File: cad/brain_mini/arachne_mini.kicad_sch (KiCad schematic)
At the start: 86 parts, among them J1 12V IN, J13 5V PI, J2 L1 servo, J3 L2 servo, J4 L3 servo, J5 L4 servo, J6 L5 servo, J7 L6 servo, J8 USB-C PI, Q1 AOD4185, SW1 RESET, SW2 BOOT, U1 TPS54560B, U10 USBLC6-2SC6, U2 AMS1117-3.3, U3 ESP32-S3-WROOM-1-N16R8, U4 74AHCT1G126, U5 74LVC1G34, U6 74AHCT1G126, U7 74LVC1G34, U8 MPU-6050

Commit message: Mini board: 2x13 GPIO header with all 19 free ESP32-S3 GPIOs + I2C + power, IMU moved
Co-Authored-By: Claude Opus 5.5 <noreply@anthropic.com>
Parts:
- added J14: GPIO, arachne:PinHeader_2x13_P2.54mm_Vertical, symbol arachne:Conn_02x13_Odd_Even
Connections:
- net 3V3: now also J14.1 (Pin_1)
- net GND: now also J14.26 (Pin_26), J14.3 (Pin_3), J14.4 (Pin_4)
- net IMU_SCL: now also J14.6 (Pin_6)
- net IMU_SDA: now also J14.5 (Pin_5)
- net V5: now also J14.2 (Pin_2)
- net IO8: now reaches U3.12 (IO8)
- net IO8: now also J14.9 (Pin_9)
- net IO3: now reaches U3.15 (IO3)
- net IO3: now also J14.10 (Pin_10)
- net IO46: now reaches U3.16 (IO46)
- net IO46: now also J14.11 (Pin_11)
- net IO12: now reaches U3.20 (IO12)
- net IO12: now also J14.12 (Pin_12)
- net IO13: now reaches U3.21 (IO13)
- net IO13: now also J14.13 (Pin_13)
- net IO14: now reaches U3.22 (IO14)
- net IO14: now also J14.14 (Pin_14)
- net IO21: now reaches U3.23 (IO21)
- net IO21: now also J14.15 (Pin_15)
- net IO47: now reaches U3.24 (IO47)
- net IO47: now also J14.16 (Pin_16)
- net IO48: now reaches U3.25 (IO48)
- net IO48: now also J14.17 (Pin_17)
- net IO45: now reaches U3.26 (IO45)
- net IO45: now also J14.18 (Pin_18)
- net IO38: now reaches U3.31 (IO38)
- net IO38: now also J14.19 (Pin_19)
- net IO39: now reaches U3.32 (IO39)
- net IO39: now also J14.20 (Pin_20)
- net IO40: now reaches U3.33 (IO40)
- net IO40: now also J14.21 (Pin_21)
- net IO41: now reaches U3.34 (IO41)
- net IO41: now also J14.22 (Pin_22)
- net IO42: now reaches U3.35 (IO42)
- net IO42: now also J14.23 (Pin_23)
- net IO44: now reaches U3.36 (RXD0)
- net IO44: now also J14.25 (Pin_25)
- net IO43: now reaches U3.37 (TXD0)
- net IO43: now also J14.24 (Pin_24)
- net IO7: now reaches U3.7 (IO7)
- net IO7: now also J14.7 (Pin_7)
- net IO15: now reaches U3.8 (IO15)
- net IO15: now also J14.8 (Pin_8)
- no-connect marks 39 -> 20
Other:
- note added: "GPIO HEADER"
- moved on the sheet: H1, H2, H3, H4

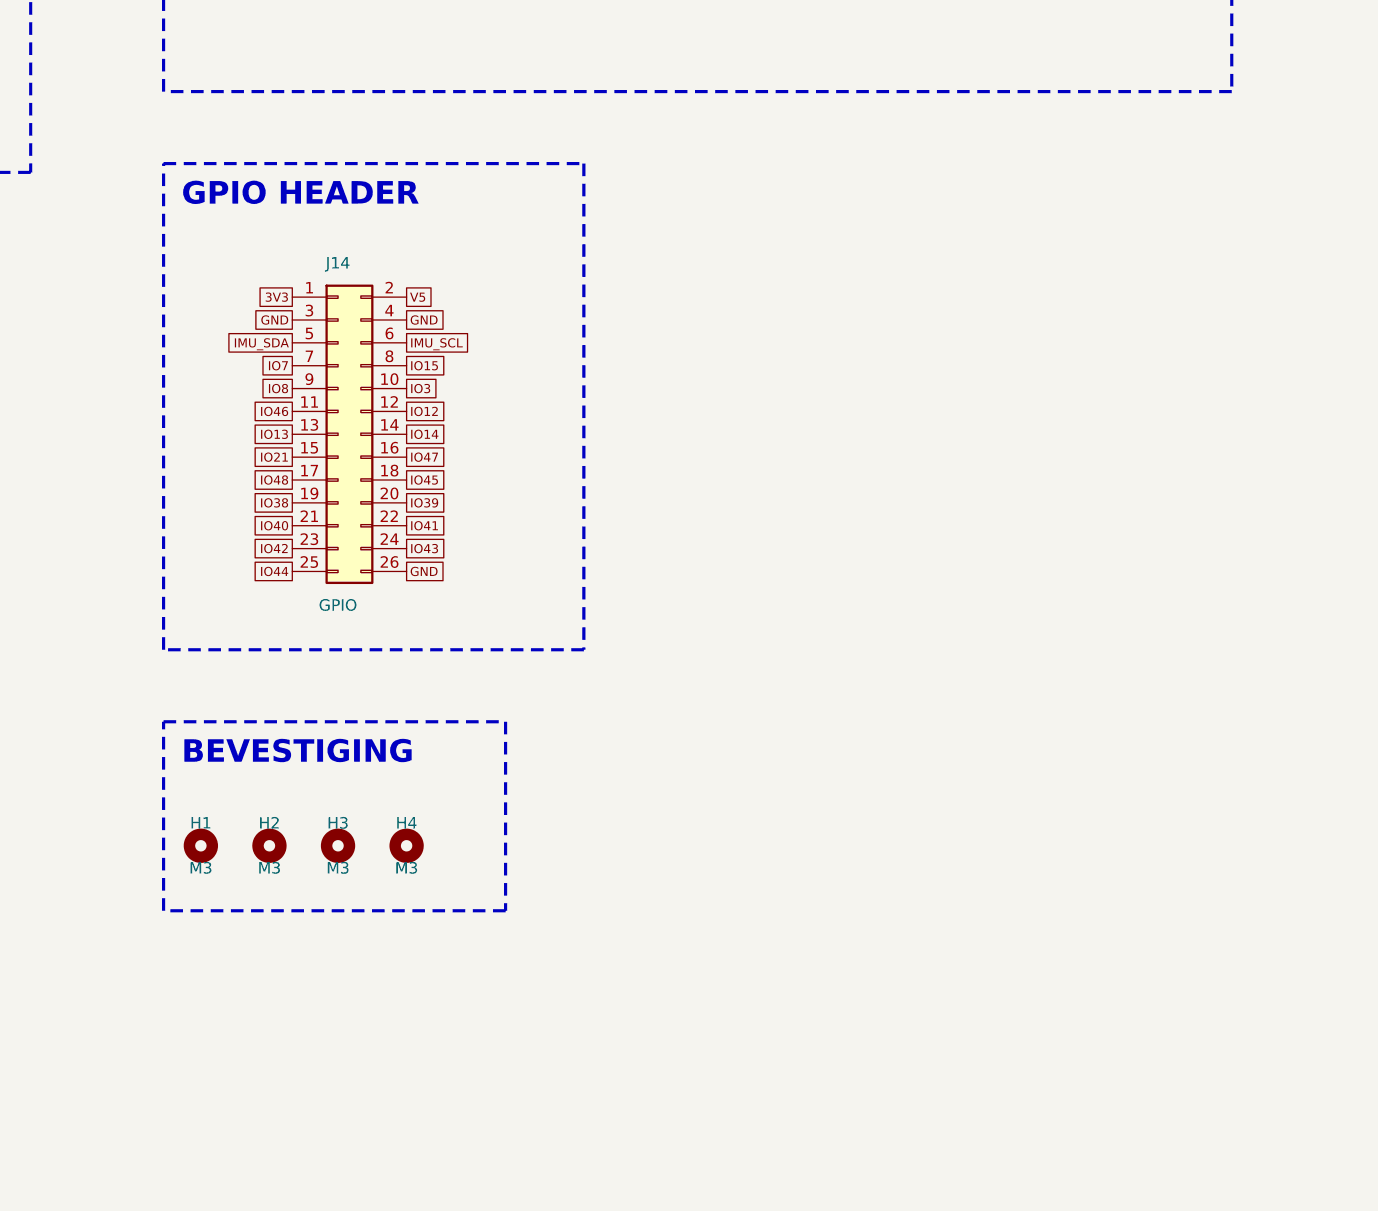
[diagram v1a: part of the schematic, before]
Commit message: Mini board: sensor strip (G-V-S per GPIO) on a 10 mm longer bottom edge, 2x Qwiic, USB-C moved to the new edge
Co-Authored-By: Claude Opus 5.5 <noreply@anthropic.com>
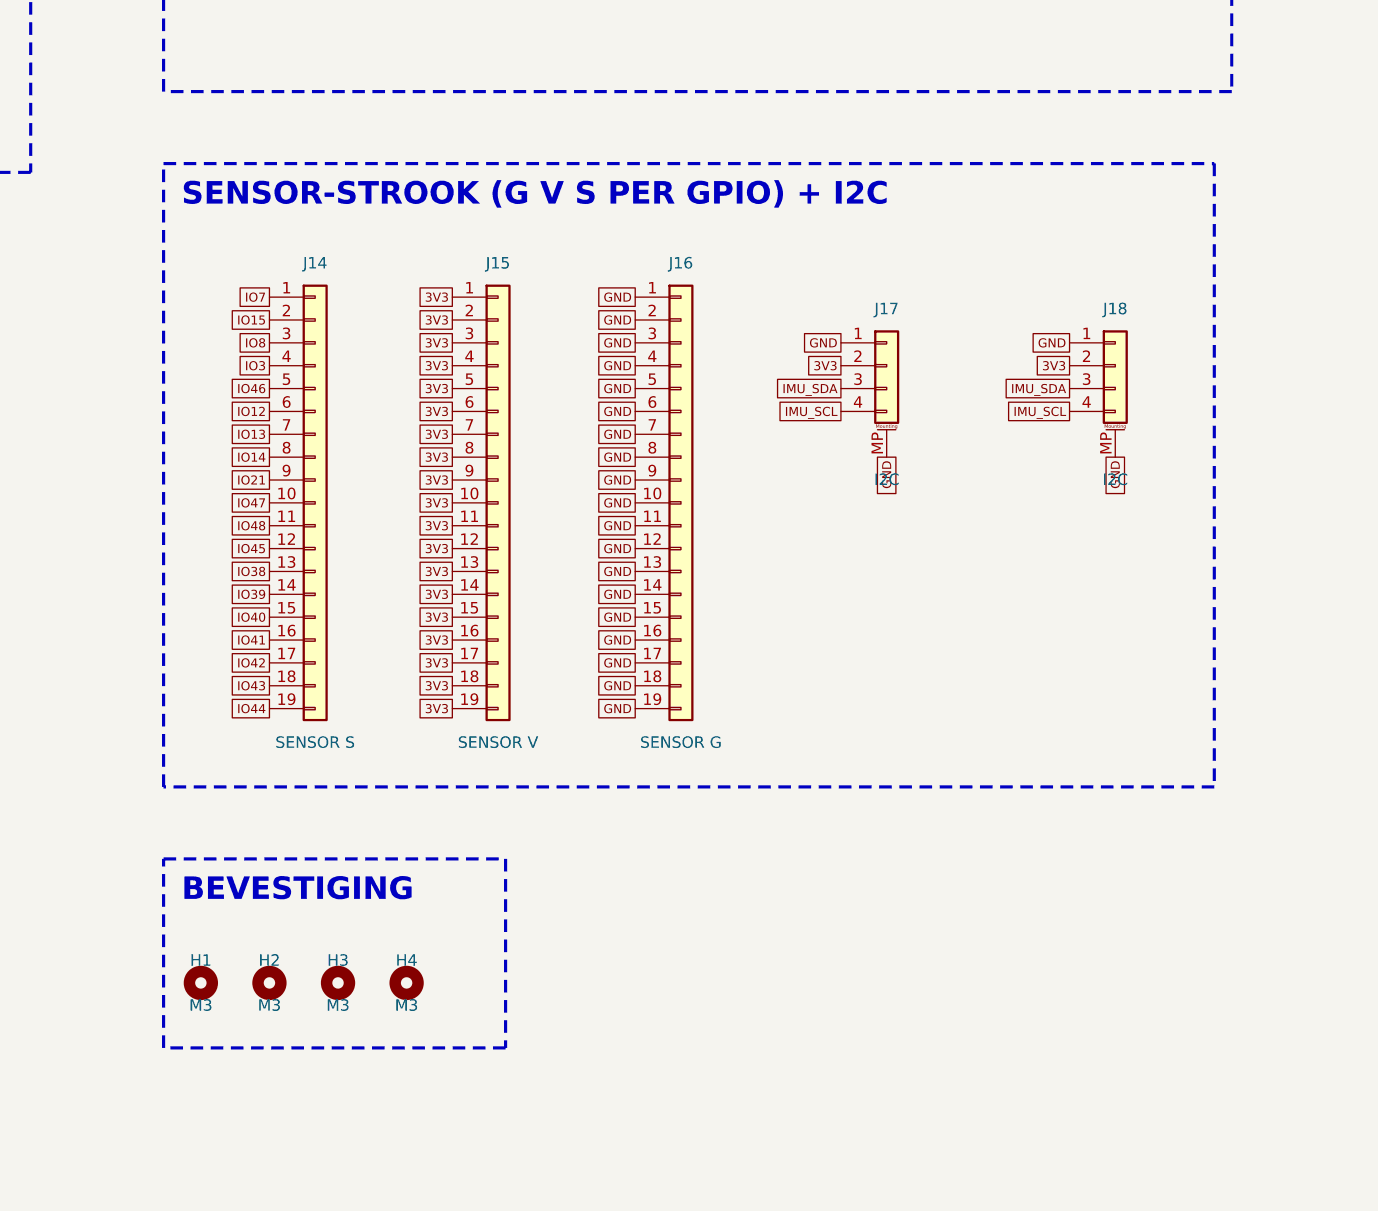
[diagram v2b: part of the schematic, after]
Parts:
- added J15: SENSOR V, arachne:PinHeader_1x19_P2.54mm_Vertical, symbol arachne:Conn_01x19
- added J16: SENSOR G, arachne:PinHeader_1x19_P2.54mm_Vertical, symbol arachne:Conn_01x19
- added J17, J18: I2C, arachne:JST_SH_SM04B-SRSS-TB_1x04-1MP_P1.00mm_Horizontal, symbol arachne:Conn_01x04_MountingPin
- J14: value GPIO -> SENSOR S; footprint arachne:PinHeader_2x13_P2.54mm_Vertical -> arachne:PinHeader_1x19_P2.54mm_Vertical; symbol arachne:Conn_02x13_Odd_Even -> arachne:Conn_01x19; MPN 2x13 pin header 2.54 mm: 19 free ESP32-S3 GPIOs + I2C + 3V3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 -> 1x19 pin header 2.54 mm (row S of the sensor strip)
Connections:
- net 3V3: now also J15.1 (Pin_1), J15.10 (Pin_10), J15.11 (Pin_11), J15.12 (Pin_12), J15.13 (Pin_13), J15.14 (Pin_14), J15.15 (Pin_15), J15.16 (Pin_16), J15.17 (Pin_17), J15.18 (Pin_18), J15.19 (Pin_19), J15.2 (Pin_2), J15.3 (Pin_3), J15.4 (Pin_4), J15.5 (Pin_5), J15.6 (Pin_6), J15.7 (Pin_7), J15.8 (Pin_8), J15.9 (Pin_9), J17.2 (Pin_2), J18.2 (Pin_2); no longer J14.1 (Pin_1)
- net GND: now also J16.1 (Pin_1), J16.10 (Pin_10), J16.11 (Pin_11), J16.12 (Pin_12), J16.13 (Pin_13), J16.14 (Pin_14), J16.15 (Pin_15), J16.16 (Pin_16), J16.17 (Pin_17), J16.18 (Pin_18), J16.19 (Pin_19), J16.2 (Pin_2), J16.3 (Pin_3), J16.4 (Pin_4), J16.5 (Pin_5), J16.6 (Pin_6), J16.7 (Pin_7), J16.8 (Pin_8), J16.9 (Pin_9), J17.1 (Pin_1), J17.MP (MountPin), J18.1 (Pin_1), J18.MP (MountPin); no longer J14.26 (Pin_26), J14.3 (Pin_3), J14.4 (Pin_4)
- net IMU_SCL: now also J17.4 (Pin_4), J18.4 (Pin_4); no longer J14.6 (Pin_6)
- net IMU_SDA: now also J17.3 (Pin_3), J18.3 (Pin_3); no longer J14.5 (Pin_5)
- net IO12: now also J14.6 (Pin_6); no longer J14.12 (Pin_12)
- net IO13: now also J14.7 (Pin_7); no longer J14.13 (Pin_13)
- net IO14: now also J14.8 (Pin_8); no longer J14.14 (Pin_14)
- net IO15: now also J14.2 (Pin_2); no longer J14.8 (Pin_8)
- net IO21: now also J14.9 (Pin_9); no longer J14.15 (Pin_15)
- net IO3: now also J14.4 (Pin_4); no longer J14.10 (Pin_10)
- net IO38: now also J14.13 (Pin_13); no longer J14.19 (Pin_19)
- net IO39: now also J14.14 (Pin_14); no longer J14.20 (Pin_20)
- net IO40: now also J14.15 (Pin_15); no longer J14.21 (Pin_21)
- net IO41: now also J14.16 (Pin_16); no longer J14.22 (Pin_22)
- net IO42: now also J14.17 (Pin_17); no longer J14.23 (Pin_23)
- net IO43: now also J14.18 (Pin_18); no longer J14.24 (Pin_24)
- net IO44: now also J14.19 (Pin_19); no longer J14.25 (Pin_25)
- net IO45: now also J14.12 (Pin_12); no longer J14.18 (Pin_18)
- net IO46: now also J14.5 (Pin_5); no longer J14.11 (Pin_11)
- net IO47: now also J14.10 (Pin_10); no longer J14.16 (Pin_16)
- net IO48: now also J14.11 (Pin_11); no longer J14.17 (Pin_17)
- net IO7: now also J14.1 (Pin_1); no longer J14.7 (Pin_7)
- net IO8: now also J14.3 (Pin_3); no longer J14.9 (Pin_9)
- net V5: no longer J14.2 (Pin_2)
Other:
- note added: "SENSOR-STROOK (G V S PER GPIO) + I2C"
- note removed: "GPIO HEADER"
- moved on the sheet: H1, H2, H3, H4

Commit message: Mini board: servo headers are now Molex Mini-SPOX 5267-03A (chamfered, mates with the 5264 plug), real Molex in the BOM
Co-Authored-By: Claude Opus 5.5 <noreply@anthropic.com>
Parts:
- J2, J3, J4, J5, J6, J7: footprint arachne:Molex_5268-03A_1x03_P2.50mm_Vertical -> arachne:Molex_5267-03A_1x03_P2.50mm_Vertical; MPN Molex 5268-03A (5264 mating, Feetech bus) -> Molex 22-03-5035 / 5267-03A Mini-SPOX (mates with the 5264 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
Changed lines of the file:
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@@
 			)
 		)
-		(property "Footprint" "arachne:Molex_5268-03A_1x03_P2.50mm_Vertical"
+		(property "Footprint" "arachne:Molex_5267-03A_1x03_P2.50mm_Vertical"
 			(at 33.02 403.86 0)
 			(effects
@@
 			)
 		)
-		(property "MPN" "Molex 5268-03A (5264 mating, Feetech bus)"
+		(property "MPN" "Molex 22-03-5035 / 5267-03A Mini-SPOX (mates with the 5264 plug on Feetech cables)"
 			(at 33.02 403.86 0)
 			(effects
@@
 			)
 		)
-		(property "Footprint" "arachne:Molex_5268-03A_1x03_P2.50mm_Vertical"
+		(property "Footprint" "arachne:Molex_5267-03A_1x03_P2.50mm_Vertical"
 			(at 53.34 403.86 0)
 			(effects
@@
 			)
 		)
-		(property "MPN" "Molex 5268-03A (5264 mating, Feetech bus)"
+		(property "MPN" "Molex 22-03-5035 / 5267-03A Mini-SPOX (mates with the 5264 plug on Feetech cables)"
 			(at 53.34 403.86 0)
 			(effects
@@
 			)
 		)
-		(property "Footprint" "arachne:Molex_5268-03A_1x03_P2.50mm_Vertical"
+		(property "Footprint" "arachne:Molex_5267-03A_1x03_P2.50mm_Vertical"
 			(at 76.2 403.86 0)
 			(effects
@@
 			)
 		)
-		(property "MPN" "Molex 5268-03A (5264 mating, Feetech bus)"
+		(property "MPN" "Molex 22-03-5035 / 5267-03A Mini-SPOX (mates with the 5264 plug on Feetech cables)"
 			(at 76.2 403.86 0)
 			(effects
@@
 			)
 		)
-		(property "Footprint" "arachne:Molex_5268-03A_1x03_P2.50mm_Vertical"
+		(property "Footprint" "arachne:Molex_5267-03A_1x03_P2.50mm_Vertical"
 			(at 33.02 482.6 0)
 			(effects
@@
 			)
 		)
-		(property "MPN" "Molex 5268-03A (5264 mating, Feetech bus)"
+		(property "MPN" "Molex 22-03-5035 / 5267-03A Mini-SPOX (mates with the 5264 plug on Feetech cables)"
 			(at 33.02 482.6 0)
 			(effects
@@
 			)
 		)
-		(property "Footprint" "arachne:Molex_5268-03A_1x03_P2.50mm_Vertical"
+		(property "Footprint" "arachne:Molex_5267-03A_1x03_P2.50mm_Vertical"
 			(at 53.34 482.6 0)
 			(effects
@@
 			)
 		)
-		(property "MPN" "Molex 5268-03A (5264 mating, Feetech bus)"
+		(property "MPN" "Molex 22-03-5035 / 5267-03A Mini-SPOX (mates with the 5264 plug on Feetech cables)"
 			(at 53.34 482.6 0)
 			(effects
@@
 			)
 		)
-		(property "Footprint" "arachne:Molex_5268-03A_1x03_P2.50mm_Vertical"
+		(property "Footprint" "arachne:Molex_5267-03A_1x03_P2.50mm_Vertical"
 			(at 76.2 482.6 0)
 			(effects
@@
 			)
 		)
-		(property "MPN" "Molex 5268-03A (5264 mating, Feetech bus)"
+		(property "MPN" "Molex 22-03-5035 / 5267-03A Mini-SPOX (mates with the 5264 plug on Feetech cables)"
 			(at 76.2 482.6 0)
 			(effects

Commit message: Name Kobe Vanrobaeys on silkscreen/schematic, fresh JLC fab files for brain_mini
Co-Authored-By: Claude Opus 5.5 <noreply@anthropic.com>
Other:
- company: Kobe Van Robaeys - maakleerplek -> Kobe Vanrobaeys - maakleerplek
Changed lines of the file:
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@@
 		(date "2026-10-18")
 		(rev "1.0")
-		(company "Kobe Van Robaeys - maakleerplek")
+		(company "Kobe Vanrobaeys - maakleerplek")
 		(comment 1 "ESP32-S3 + MPU-6050, 6 servo-bus legs, USB to Pi 4")
 	)

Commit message: brain_mini v4 price pass: JLC basic parts (buck network, caps, SS54, LEDs), LSM6DS3TR-C IMU, hand-solder parts DNP, JLC rotation corrections in the CPL
Co-Authored-By: Claude Opus 5.5 <noreply@anthropic.com>
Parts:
- removed C25: 2n2, arachne:C_0603_1608Metric, symbol arachne:C
- removed C27: 10n, arachne:C_0603_1608Metric, symbol arachne:C
- C1, C2: MPN 330uF 25V 8x10.5 alu -> hand-solder (not placed by JLC): 330uF 25V 8x10.5 alu, STRO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; now not fitted
- C10, C11, C9: footprint arachne:C_1210_3225Metric -> arachne:C_1206_3216Metric; MPN 1210 47u 10V X5R ceramic -> 1206 47u 10V X5R ceramic
- C3, C5, C6: footprint arachne:C_1206_3216Metric -> arachne:C_0805_2012Metric; MPN 1206 10u 25V X5R ceramic -> 0805 10u 25V X5R ceramic
- D1: MPN SMBJ15CA -> hand-solder (not placed by JLC): SMBJ15CA TVS (optional); now not fitted
- D2: MPN BZT52C15 (gate clamp) -> hand-solder (not placed by JLC): BZT52C15 gate clamp (optio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; now not fitted
- D4: value B560C -> SS54; footprint arachne:D_SMC -> arachne:D_SMA; MPN B560C (5 A 60 V Schottky) -> SS54 (5 A 40 V Schottky, JLC basic)
- D5: value groen 5V -> LED 5V; MPN LED 0603 green -> LED 0603 red (JLC basic)
- D8: value blauw ESP -> LED ESP; MPN LED 0603 blue -> LED 0603 red (JLC basic)
- J14: MPN 1x19 pin header 2.54 mm (row S of the sensor strip) -> hand-solder (not placed by JLC): 1x19 pin header 2.54 mm (r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; now not fitted
- J15: MPN 1x19 pin header 2.54 mm (row V of the sensor strip) -> hand-solder (not placed by JLC): 1x19 pin header 2.54 mm (r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; now not fitted
- J16: MPN 1x19 pin header 2.54 mm (row G of the sensor strip) -> hand-solder (not placed by JLC): 1x19 pin header 2.54 mm (r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; now not fitted
- J17, J18: MPN JST SM04B-SRSS-TB (Qwiic / STEMMA QT) -> hand-solder (not placed by JLC): JST SM04B-SRSS-TB (Qwiic /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; now not fitted
- J2, J3, J4, J5, J6, J7: MPN Molex 22-03-5035 / 5267-03A Mini-SPOX (mates with the 5264 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 -> hand-solder (not placed by JLC): Molex 22-03-5035 / 5267-03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; now not fitted
- R4: value 442k -> 470k; MPN 0603 442k 1% -> 0603 470k 1%
- R5: value 90.9k -> 100k; MPN 0603 90.9k 1% -> 0603 100k 1%
- R6: value 243k -> 220k; MPN 0603 243k 1% -> 0603 220k 1%
- R7: value 53.6k -> 27k; MPN 0603 53.6k 1% -> 0603 27k 1%
- R8: value 10.2k -> 5k1; MPN 0603 10.2k 1% -> 0603 5k1 1%
- R9: value 16.9k -> 15k; MPN 0603 16.9k 1% -> 0603 15k 1%
- SW1, SW2: MPN CK KMR221G (4.2x2.8 tact) -> hand-solder (not placed by JLC): CK KMR221G (4.2x2.8 tact);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; now not fitted
- U10: MPN USBLC6-2SC6 -> hand-solder (not placed by JLC): USBLC6-2SC6 ESD (optional); now not fitted
- U8: value MPU-6050 -> LSM6DS3TR-C; footprint arachne:InvenSense_QFN-24_4x4mm_P0.5mm -> arachne:LGA-14_3x2.5mm_P0.5mm_LayoutBorder3x4y; symbol arachne:MPU-6050 -> arachne:LSM6DS3; MPN MPU-6050 -> LSM6DS3TR-C (6-axis IMU, I2C 0x6A)
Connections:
- net 3V3: now also C24.1, U8.12 (CS), U8.5 (VDDIO); no longer U8.13 (VDD)
- net GND: now also U8.2 (SDX), U8.3 (SCX), U8.6 (GND), U8.7 (GND); no longer U8.11 (FSYNC), U8.18 (GND), U8.9 (AD0)
- net IMU_INT: now also U8.4 (INT1); no longer U8.12 (INT)
- net IMU_SCL: now also U8.13 (SCL); no longer U8.23 (SCL)
- net IMU_SDA: now also U8.14 (SDA); no longer U8.24 (SDA)
- removed net IMU_CP: U8.20 (CPOUT)
- net IMU_REG: no longer names the net of U8.10 (NC)
- net IMU_REG: no longer C24.1
- no-connect marks 20 -> 10
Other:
- note added: "IMU LSM6DS3TR-C"
- note removed: "IMU MPU-6050"
- moved on the sheet: C24, C26, C29, H1, H2, H3, H4, J8, R24, R25, R27, R28
